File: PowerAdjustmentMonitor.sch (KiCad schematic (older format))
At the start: 18 parts, among them U3 LM317K, U4 7805, U5 7805, U6 LM317K, U7 LM324

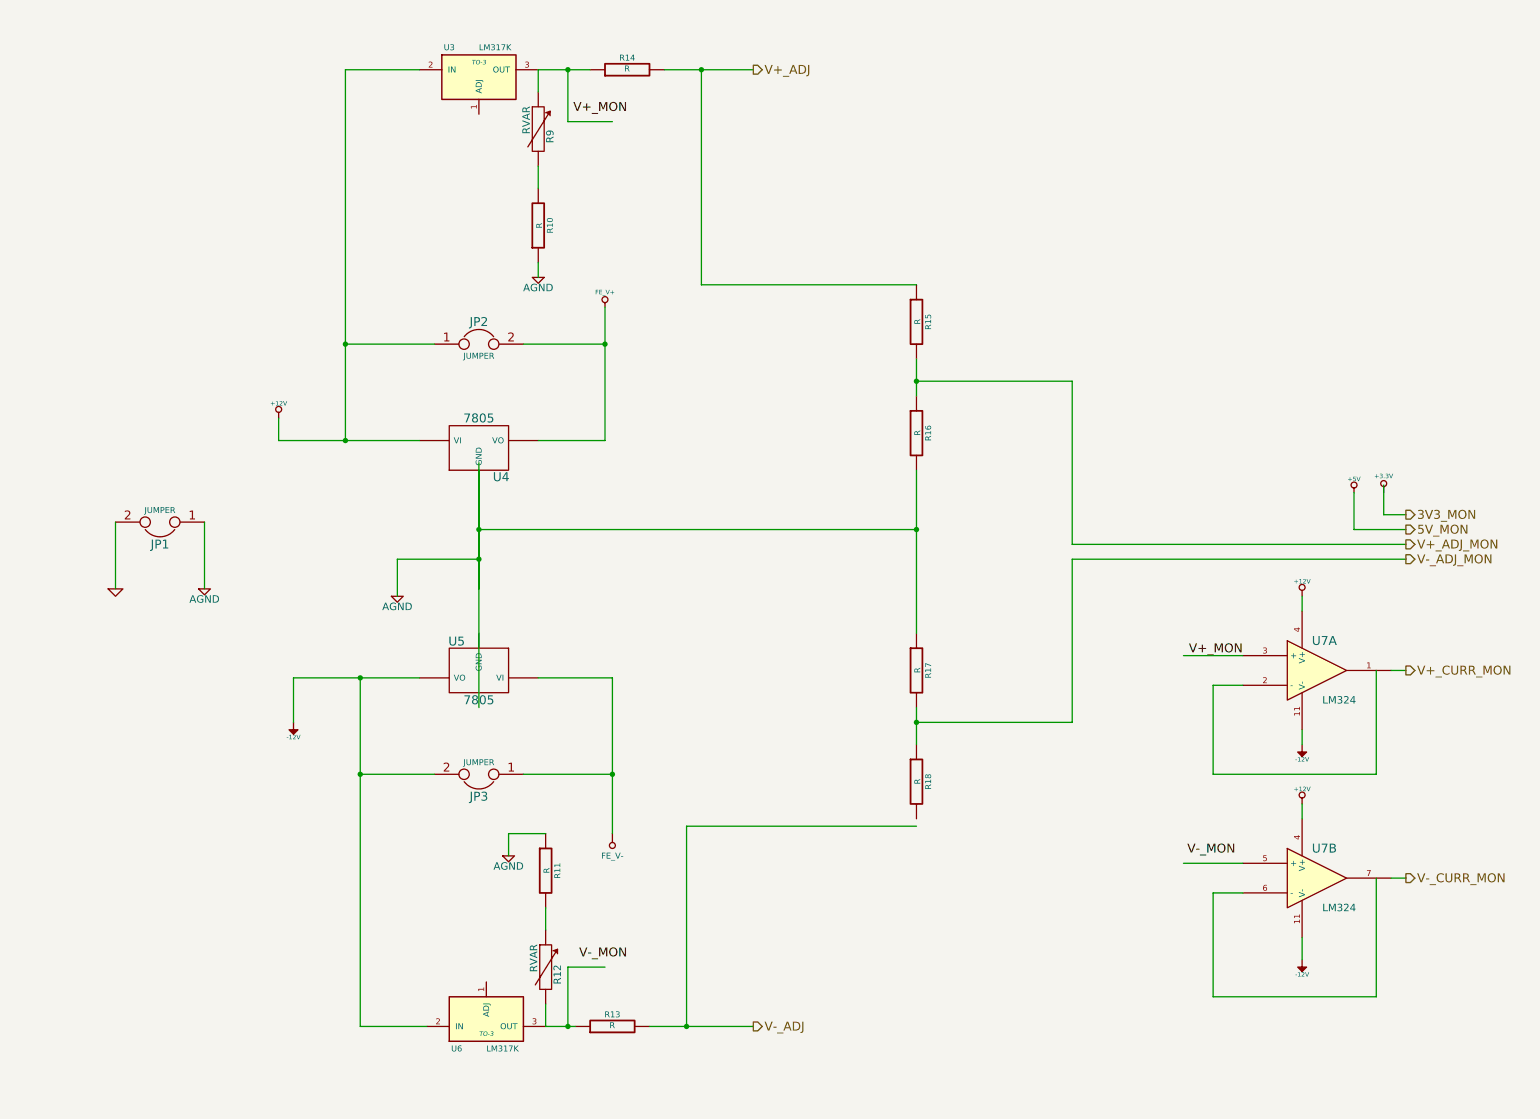
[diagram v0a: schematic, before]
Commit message: 5.4 Video 1/2 Associating and Placing the Thermocouple Module
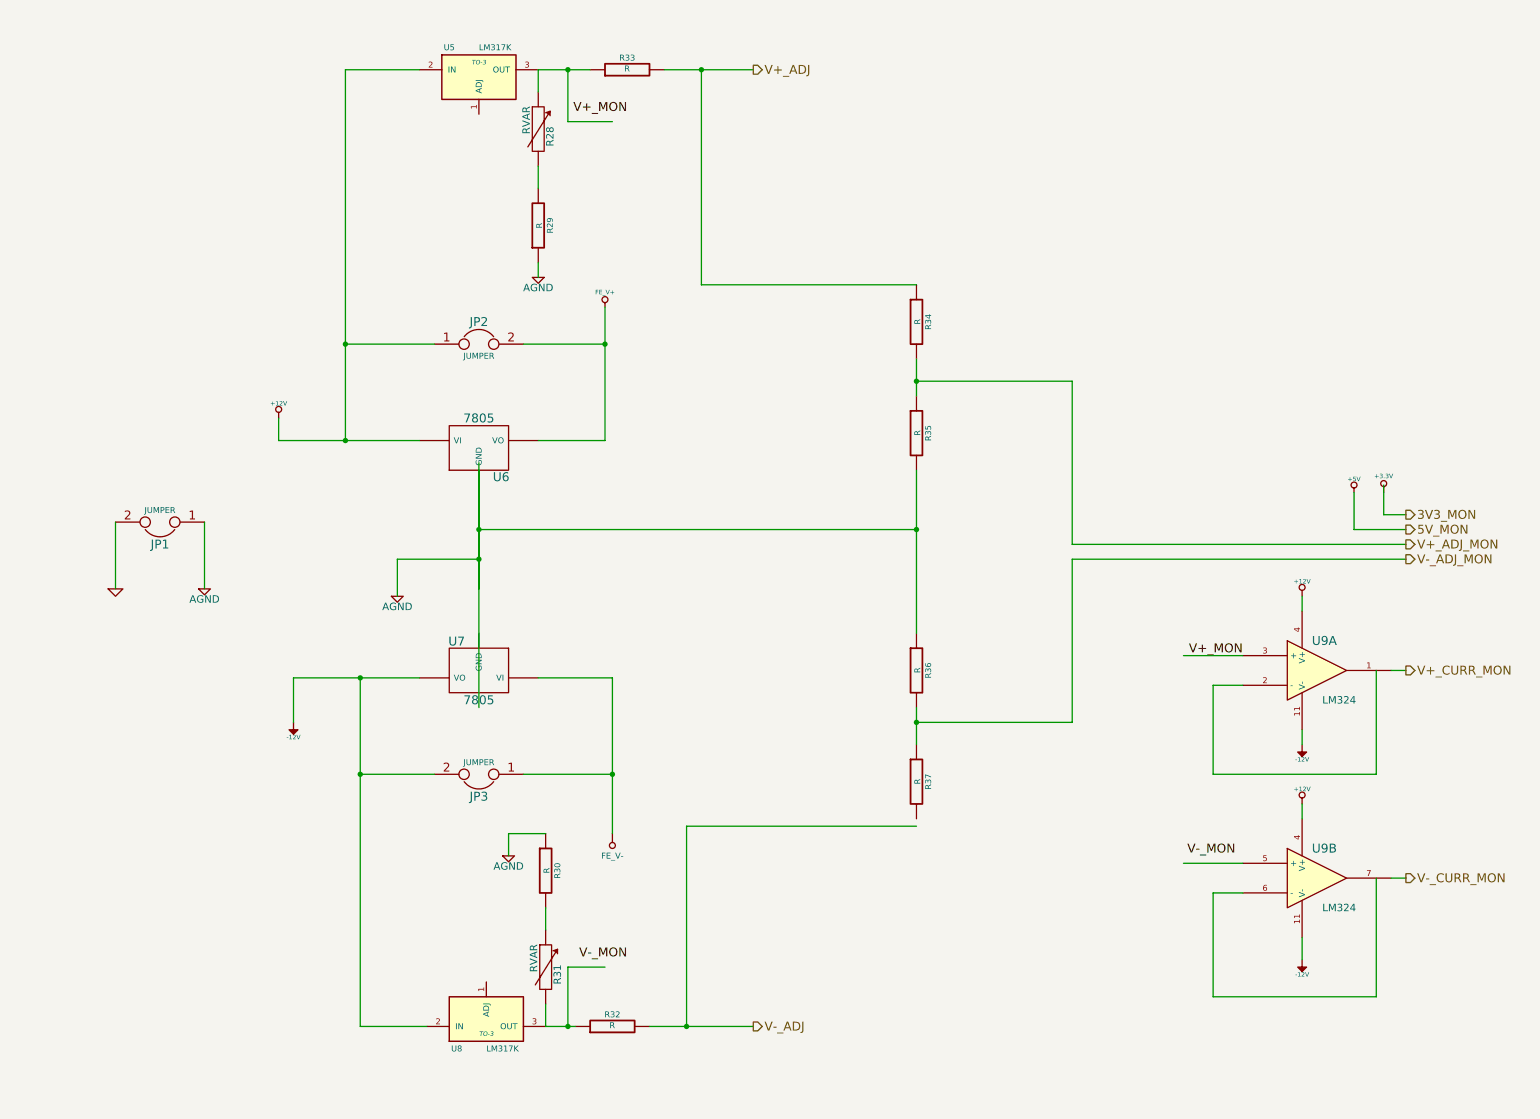
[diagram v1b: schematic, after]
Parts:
- renumbered R9 to R28, R10 to R29, R11 to R30, R12 to R31, R13 to R32, R14 to R33, R15 to R34, R16 to R35, R17 to R36, R18 to R37, U3 to U5, U4 to U6, U5 to U7, U6 to U8, U7 to U9
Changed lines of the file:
@@
 Sheet 9 9
 Title ""
-Date "19 feb 2014"
+Date "21 feb 2014"
 Rev ""
 Comp ""
@@
 $EndDescr
 $Comp
-L 7805 U4
+L 7805 U6
 U 1 1 52F50F52
 P 3850 3350
-F 0 "U4" H 4000 3154 60  0000 C CNN
+F 0 "U6" H 4000 3154 60  0000 C CNN
 F 1 "7805" H 3850 3550 60  0000 C CNN
 F 2 "" H 3850 3350 60  0000 C CNN
@@
 $EndComp
 $Comp
-L 7805 U5
+L 7805 U7
 U 1 1 52F50F5F
 P 3850 4850
-F 0 "U5" H 4000 4654 60  0000 C CNN
+F 0 "U7" H 4000 4654 60  0000 C CNN
 F 1 "7805" H 3850 5050 60  0000 C CNN
 F 2 "" H 3850 4850 60  0000 C CNN
@@
 $EndComp
 $Comp
-L R R11
+L R R30
 U 1 1 52F50F76
 P 4300 6200
-F 0 "R11" V 4380 6200 40  0000 C CNN
+F 0 "R30" V 4380 6200 40  0000 C CNN
 F 1 "R" V 4307 6201 40  0000 C CNN
 F 2 "" V 4230 6200 30  0000 C CNN
@@
 $EndComp
 $Comp
-L GND #PWR020
+L GND #PWR27
 U 1 1 52F50FA0
 P 1400 4300
-F 0 "#PWR020" H 1400 4300 30  0001 C CNN
+F 0 "#PWR27" H 1400 4300 30  0001 C CNN
 F 1 "GND" H 1400 4230 30  0001 C CNN
 F 2 "" H 1400 4300 60  0000 C CNN
@@
 $EndComp
 $Comp
-L AGND #PWR021
+L AGND #PWR28
 U 1 1 52F50FB9
 P 2000 4300
-F 0 "#PWR021" H 2000 4300 40  0001 C CNN
+F 0 "#PWR28" H 2000 4300 40  0001 C CNN
 F 1 "AGND" H 2000 4230 50  0000 C CNN
 F 2 "" H 2000 4300 60  0000 C CNN
@@
 $EndComp
 $Comp
-L AGND #PWR022
+L AGND #PWR31
 U 1 1 52F50FF4
 P 3300 4350
-F 0 "#PWR022" H 3300 4350 40  0001 C CNN
+F 0 "#PWR31" H 3300 4350 40  0001 C CNN
 F 1 "AGND" H 3300 4280 50  0000 C CNN
 F 2 "" H 3300 4350 60  0000 C CNN
@@
 $EndComp
 $Comp
-L +12V #PWR023
+L +12V #PWR29
 U 1 1 52F5102D
 P 2500 3150
-F 0 "#PWR023" H 2500 3100 20  0001 C CNN
+F 0 "#PWR29" H 2500 3100 20  0001 C CNN
 F 1 "+12V" H 2500 3250 30  0000 C CNN
 F 2 "" H 2500 3150 60  0000 C CNN
@@
 $EndComp
 $Comp
-L -12V #PWR024
+L -12V #PWR30
 U 1 1 52F5104F
 P 2600 5200
-F 0 "#PWR024" H 2600 5330 20  0001 C CNN
+F 0 "#PWR30" H 2600 5330 20  0001 C CNN
 F 1 "-12V" H 2600 5300 30  0000 C CNN
 F 2 "" H 2600 5200 60  0000 C CNN
@@
 $EndComp
 $Comp
-L FE_V+ #PWR025
+L FE_V+ #PWR34
 U 1 1 52F5159F
 P 4700 2400
-F 0 "#PWR025" H 4700 2500 30  0001 C CNN
+F 0 "#PWR34" H 4700 2500 30  0001 C CNN
 F 1 "FE_V+" H 4700 2500 30  0000 C CNN
 F 2 "" H 4700 2400 60  0000 C CNN
@@
 $EndComp
 $Comp
-L FE_V- #PWR28
+L FE_V- #PWR35
 U 1 1 52F515C8
 P 4750 5950
-F 0 "#PWR28" H 4750 6150 40  0001 C CNN
+F 0 "#PWR35" H 4750 6150 40  0001 C CNN
 F 1 "FE_V-" H 4750 6100 40  0000 C CNN
 F 2 "" H 4750 5950 60  0000 C CNN
@@
 $EndComp
 $Comp
-L LM317K U6
+L LM317K U8
 U 1 1 52F51657
 P 3900 7200
-F 0 "U6" H 3700 7400 40  0000 C CNN
+F 0 "U8" H 3700 7400 40  0000 C CNN
 F 1 "LM317K" H 3900 7400 40  0000 L CNN
 F 2 "TO-3" H 3900 7300 30  0000 C CIN
@@
 $EndComp
 $Comp
-L AGND #PWR026
+L AGND #PWR32
 U 1 1 52F516D6
 P 4050 6100
-F 0 "#PWR026" H 4050 6100 40  0001 C CNN
+F 0 "#PWR32" H 4050 6100 40  0001 C CNN
 F 1 "AGND" H 4050 6030 50  0000 C CNN
 F 2 "" H 4050 6100 60  0000 C CNN
@@
 $EndComp
 $Comp
-L R R10
+L R R29
 U 1 1 52F51728
 P 4250 1850
-F 0 "R10" V 4330 1850 40  0000 C CNN
+F 0 "R29" V 4330 1850 40  0000 C CNN
 F 1 "R" V 4257 1851 40  0000 C CNN
 F 2 "" V 4180 1850 30  0000 C CNN
@@
 $EndComp
 $Comp
-L LM317K U3
+L LM317K U5
 U 1 1 52F5172F
 P 3850 850
-F 0 "U3" H 3650 1050 40  0000 C CNN
+F 0 "U5" H 3650 1050 40  0000 C CNN
 F 1 "LM317K" H 3850 1050 40  0000 L CNN
 F 2 "TO-3" H 3850 950 30  0000 C CIN
@@
 $EndComp
 $Comp
-L AGND #PWR027
+L AGND #PWR33
 U 1 1 52F51738
 P 4250 2200
-F 0 "#PWR027" H 4250 2200 40  0001 C CNN
+F 0 "#PWR33" H 4250 2200 40  0001 C CNN
 F 1 "AGND" H 4250 2130 50  0000 C CNN
 F 2 "" H 4250 2200 60  0000 C CNN
@@
 V-_ADJ
 $Comp
-L +3.3V #PWR028
+L +3.3V #PWR41
 U 1 1 52F517F0
 P 9950 3650
-F 0 "#PWR028" H 9950 3610 30  0001 C CNN
+F 0 "#PWR41" H 9950 3610 30  0001 C CNN
 F 1 "+3.3V" H 9950 3760 30  0000 C CNN
 F 2 "" H 9950 3650 60  0000 C CNN
@@
 V-_ADJ_MON
 $Comp
-L +5V #PWR029
+L +5V #PWR40
 U 1 1 52F51806
 P 9750 3650
-F 0 "#PWR029" H 9750 3740 20  0001 C CNN
+F 0 "#PWR40" H 9750 3740 20  0001 C CNN
 F 1 "+5V" H 9750 3740 30  0000 C CNN
 F 2 "" H 9750 3650 60  0000 C CNN
@@
 V-_CURR_MON
 $Comp
-L R R15
+L R R34
 U 1 1 52F5181A
 P 6800 2500
-F 0 "R15" V 6880 2500 40  0000 C CNN
+F 0 "R34" V 6880 2500 40  0000 C CNN
 F 1 "R" V 6807 2501 40  0000 C CNN
 F 2 "" V 6730 2500 30  0000 C CNN
@@
 $EndComp
 $Comp
-L R R16
+L R R35
 U 1 1 52F5182D
 P 6800 3250
-F 0 "R16" V 6880 3250 40  0000 C CNN
+F 0 "R35" V 6880 3250 40  0000 C CNN
 F 1 "R" V 6807 3251 40  0000 C CNN
 F 2 "" V 6730 3250 30  0000 C CNN
@@
 	6800 2750 6800 3000
 $Comp
-L R R17
+L R R36
 U 1 1 52F51905
 P 6800 4850
-F 0 "R17" V 6880 4850 40  0000 C CNN
+F 0 "R36" V 6880 4850 40  0000 C CNN
 F 1 "R" V 6807 4851 40  0000 C CNN
 F 2 "" V 6730 4850 30  0000 C CNN
@@
 $EndComp
 $Comp
-L R R18
+L R R37
 U 1 1 52F5190B
 P 6800 5600
-F 0 "R18" V 6880 5600 40  0000 C CNN
+F 0 "R37" V 6880 5600 40  0000 C CNN
 F 1 "R" V 6807 5601 40  0000 C CNN
 F 2 "" V 6730 5600 30  0000 C CNN
@@
 	9750 3900 10100 3900
 $Comp
-L R R13
+L R R32
 U 1 1 52F51ABE
 P 4750 7250
-F 0 "R13" V 4830 7250 40  0000 C CNN
+F 0 "R32" V 4830 7250 40  0000 C CNN
 F 1 "R" V 4757 7251 40  0000 C CNN
 F 2 "" V 4680 7250 30  0000 C CNN
@@
 	4300 7250 4500 7250
 $Comp
-L R R14
+L R R33
 U 1 1 52F51B5C
 P 4850 800
-F 0 "R14" V 4930 800 40  0000 C CNN
+F 0 "R33" V 4930 800 40  0000 C CNN
 F 1 "R" V 4857 801 40  0000 C CNN
 F 2 "" V 4780 800 30  0000 C CNN
@@
 V+_MON
 $Comp
-L LM324 U7
+L LM324 U9
 U 1 1 52F51E74
 P 9500 4850
-F 0 "U7" H 9550 5050 60  0000 C CNN
+F 0 "U9" H 9550 5050 60  0000 C CNN
 F 1 "LM324" H 9650 4650 50  0000 C CNN
 F 2 "" H 9500 4850 60  0000 C CNN
@@
 $EndComp
 $Comp
-L LM324 U7
+L LM324 U9
 U 2 1 52F51E7A
 P 9500 6250
-F 0 "U7" H 9550 6450 60  0000 C CNN
+F 0 "U9" H 9550 6450 60  0000 C CNN
 F 1 "LM324" H 9650 6050 50  0000 C CNN
 F 2 "" H 9500 6250 60  0000 C CNN
@@
 	10000 6250 10100 6250
 $Comp
-L +12V #PWR030
+L +12V #PWR36
 U 1 1 52F51F5F
 P 9400 4350
-F 0 "#PWR030" H 9400 4300 20  0001 C CNN
+F 0 "#PWR36" H 9400 4300 20  0001 C CNN
 F 1 "+12V" H 9400 4450 30  0000 C CNN
 F 2 "" H 9400 4350 60  0000 C CNN
@@
 	9400 4350 9400 4450
 $Comp
-L +12V #PWR031
+L +12V #PWR38
 U 1 1 52F51FC1
 P 9400 5750
-F 0 "#PWR031" H 9400 5700 20  0001 C CNN
+F 0 "#PWR38" H 9400 5700 20  0001 C CNN
 F 1 "+12V" H 9400 5850 30  0000 C CNN
 F 2 "" H 9400 5750 60  0000 C CNN
@@
 	9400 5750 9400 5850
 $Comp
-L -12V #PWR032
+L -12V #PWR37
 U 1 1 52F5201F
 P 9400 5350
-F 0 "#PWR032" H 9400 5480 20  0001 C CNN
+F 0 "#PWR37" H 9400 5480 20  0001 C CNN
 F 1 "-12V" H 9400 5450 30  0000 C CNN
 F 2 "" H 9400 5350 60  0000 C CNN
@@
 	9400 5250 9400 5350
 $Comp
-L -12V #PWR033
+L -12V #PWR39
 U 1 1 52F5207B
 P 9400 6800
-F 0 "#PWR033" H 9400 6930 20  0001 C CNN
+F 0 "#PWR39" H 9400 6930 20  0001 C CNN
 F 1 "-12V" H 9400 6900 30  0000 C CNN
 F 2 "" H 9400 6800 60  0000 C CNN
@@
 V-_MON
 $Comp
-L RVAR R12
+L RVAR R31
 U 1 1 52F526E6
 P 4300 6850
-F 0 "R12" V 4380 6800 50  0000 C CNN
+F 0 "R31" V 4380 6800 50  0000 C CNN
 F 1 "RVAR" V 4220 6910 50  0000 C CNN
 F 2 "" H 4300 6850 60  0000 C CNN
@@
 $EndComp
 $Comp
-L RVAR R9
+L RVAR R28
 U 1 1 52F526F3
 P 4250 1200
-F 0 "R9" V 4330 1150 50  0000 C CNN
+F 0 "R28" V 4330 1150 50  0000 C CNN
 F 1 "RVAR" V 4170 1260 50  0000 C CNN
 F 2 "" H 4250 1200 60  0000 C CNN

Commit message: 5.10 Video 1/2 Associating and Placing the Power Modification Module
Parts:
- removed JP2, JP3: JUMPER, symbol JUMPER
- removed U6, U7: 7805, symbol 7805
- removed U8: LM317K, TO-3, symbol LM317K
- removed U9: LM324, symbol LM324
- added C14, C15, C16, C17, C18, C19, C20, C21, C22, C23, C24, C25: C, ~, symbol C
- added D10, D5, D6, D7, D8, D9: DIODE, ~, symbol DIODE
- added R54, R55: R, ~, symbol R
- added U6, U7: LM337T, TO-220, symbol LM337T
- added U8: LM317, ~, symbol LM317
- R30, R32, R33: footprint (none) -> ~
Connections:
- net labels removed: V+_CURR_MON, V-_CURR_MON, V-_MON
- wire segments 71 -> 93
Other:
- note added: "- 1.5 to 10V Output"
- note added: "-10V Output"
- note added: "1.5 to 10 V Output"
- note added: "10V Output"
- moved on the sheet: JP1, R28, R29

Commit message: 5.10 Video 2/2 Associating and Placing the Power Modification Module
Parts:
- added D11, D12: MMBD914-7-F, ~, symbol DIODE
- D10, D5, D6, D7, D8, D9: value DIODE -> MMBD914-7-F
- R28: value RVAR -> 5K
- R29, R30: value R -> 715
- R31: value RVAR -> 5k
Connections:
- wire segments 93 -> 101
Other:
- moved on the sheet: D7
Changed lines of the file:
@@
 Sheet 8 9
 Title ""
-Date "23 feb 2014"
+Date "24 feb 2014"
 Rev ""
 Comp ""
@@
 $EndComp
 $Comp
-L GND #PWR39
+L GND #PWR038
 U 1 1 52F50FA0
 P 800 3900
-F 0 "#PWR39" H 800 3900 30  0001 C CNN
+F 0 "#PWR038" H 800 3900 30  0001 C CNN
 F 1 "GND" H 800 3830 30  0001 C CNN
 F 2 "" H 800 3900 60  0000 C CNN
@@
 $EndComp
 $Comp
-L AGND #PWR40
+L AGND #PWR039
 U 1 1 52F50FB9
 P 1400 3900
-F 0 "#PWR40" H 1400 3900 40  0001 C CNN
+F 0 "#PWR039" H 1400 3900 40  0001 C CNN
 F 1 "AGND" H 1400 3830 50  0000 C CNN
 F 2 "" H 1400 3900 60  0000 C CNN
@@
 $EndComp
 $Comp
-L AGND #PWR42
+L AGND #PWR040
 U 1 1 52F50FF4
 P 2300 4150
-F 0 "#PWR42" H 2300 4150 40  0001 C CNN
+F 0 "#PWR040" H 2300 4150 40  0001 C CNN
 F 1 "AGND" H 2300 4080 50  0000 C CNN
 F 2 "" H 2300 4150 60  0000 C CNN
@@
 $EndComp
 $Comp
-L +12V #PWR41
+L +12V #PWR041
 U 1 1 52F5102D
 P 2300 650
-F 0 "#PWR41" H 2300 600 20  0001 C CNN
+F 0 "#PWR041" H 2300 600 20  0001 C CNN
 F 1 "+12V" H 2300 750 30  0000 C CNN
 F 2 "" H 2300 650 60  0000 C CNN
@@
 $EndComp
 $Comp
-L -12V #PWR43
+L -12V #PWR042
 U 1 1 52F5104F
 P 2300 5350
-F 0 "#PWR43" H 2300 5480 20  0001 C CNN
+F 0 "#PWR042" H 2300 5480 20  0001 C CNN
 F 1 "-12V" H 2300 5450 30  0000 C CNN
 F 2 "" H 2300 5350 60  0000 C CNN
@@
 P 4300 1200
 F 0 "R29" V 4380 1200 40  0000 C CNN
-F 1 "R" V 4307 1201 40  0000 C CNN
+F 1 "715" V 4307 1201 40  0000 C CNN
 F 2 "" V 4230 1200 30  0000 C CNN
 F 3 "" H 4300 1200 30  0000 C CNN
@@
 $EndComp
 $Comp
-L AGND #PWR46
+L AGND #PWR043
 U 1 1 52F51738
 P 4300 2200
-F 0 "#PWR46" H 4300 2200 40  0001 C CNN
+F 0 "#PWR043" H 4300 2200 40  0001 C CNN
 F 1 "AGND" H 4300 2130 50  0000 C CNN
 F 2 "" H 4300 2200 60  0000 C CNN
@@
 V-_ADJ
 $Comp
-L +3.3V #PWR50
+L +3.3V #PWR044
 U 1 1 52F517F0
 P 9950 3650
-F 0 "#PWR50" H 9950 3610 30  0001 C CNN
+F 0 "#PWR044" H 9950 3610 30  0001 C CNN
 F 1 "+3.3V" H 9950 3760 30  0000 C CNN
 F 2 "" H 9950 3650 60  0000 C CNN
@@
 V-_ADJ_MON
 $Comp
-L +5V #PWR49
+L +5V #PWR045
 U 1 1 52F51806
 P 9750 3650
-F 0 "#PWR49" H 9750 3740 20  0001 C CNN
+F 0 "#PWR045" H 9750 3740 20  0001 C CNN
 F 1 "+5V" H 9750 3740 30  0000 C CNN
 F 2 "" H 9750 3650 60  0000 C CNN
@@
 P 4300 1850
 F 0 "R28" V 4380 1800 50  0000 C CNN
-F 1 "RVAR" V 4220 1910 50  0000 C CNN
+F 1 "5K" V 4220 1910 50  0000 C CNN
 F 2 "" H 4300 1850 60  0000 C CNN
 F 3 "" H 4300 1850 60  0000 C CNN
@@
 $EndComp
 $Comp
-L FE_V+ #PWR47
+L FE_V+ #PWR046
 U 1 1 530A7BE6
 P 5150 2550
-F 0 "#PWR47" H 5150 2650 30  0001 C CNN
+F 0 "#PWR046" H 5150 2650 30  0001 C CNN
 F 1 "FE_V+" H 5150 2650 30  0000 C CNN
 F 2 "~" H 5150 2550 60  0000 C CNN
@@
 Text Notes 4250 600  0    60   ~ 0
 1.5 to 10 V Output
-Text Notes 5050 2800 0    60   ~ 0
+Text Notes 5250 2550 0    60   ~ 0
 10V Output
 $Comp
@@
 P 3950 7150
 F 0 "R30" V 4030 7150 40  0000 C CNN
-F 1 "R" V 3957 7151 40  0000 C CNN
+F 1 "715" V 3957 7151 40  0000 C CNN
 F 2 "~" V 3880 7150 30  0000 C CNN
 F 3 "~" H 3950 7150 30  0000 C CNN
@@
 $EndComp
 $Comp
-L AGND #PWR45
+L AGND #PWR047
 U 1 1 530A7F80
 P 3400 6250
-F 0 "#PWR45" H 3400 6250 40  0001 C CNN
+F 0 "#PWR047" H 3400 6250 40  0001 C CNN
 F 1 "AGND" H 3400 6180 50  0000 C CNN
 F 2 "" H 3400 6250 60  0000 C CNN
@@
 P 3950 6400
 F 0 "R31" V 4030 6350 50  0000 C CNN
-F 1 "RVAR" V 3870 6460 50  0000 C CNN
+F 1 "5k" V 3870 6460 50  0000 C CNN
 F 2 "" H 3950 6400 60  0000 C CNN
 F 3 "" H 3950 6400 60  0000 C CNN
@@
 $EndComp
 $Comp
-L AGND #PWR44
+L AGND #PWR048
 U 1 1 530A8E3E
 P 3000 1600
-F 0 "#PWR44" H 3000 1600 40  0001 C CNN
+F 0 "#PWR048" H 3000 1600 40  0001 C CNN
 F 1 "AGND" H 3000 1530 50  0000 C CNN
 F 2 "" H 3000 1600 60  0000 C CNN
@@
 P 4650 1150
 F 0 "D9" H 4650 1250 40  0000 C CNN
-F 1 "DIODE" H 4650 1050 40  0000 C CNN
+F 1 "MMBD914-7-F" H 4650 1050 40  0000 C CNN
 F 2 "~" H 4650 1150 60  0000 C CNN
 F 3 "~" H 4650 1150 60  0000 C CNN
@@
 P 3850 550
 F 0 "D5" H 3850 650 40  0000 C CNN
-F 1 "DIODE" H 3850 450 40  0000 C CNN
+F 1 "MMBD914-7-F" H 3850 450 40  0000 C CNN
 F 2 "~" H 3850 550 60  0000 C CNN
 F 3 "~" H 3850 550 60  0000 C CNN
@@
 P 4050 2400
 F 0 "D6" H 4050 2500 40  0000 C CNN
-F 1 "DIODE" H 4050 2300 40  0000 C CNN
+F 1 "MMBD914-7-F" H 4050 2300 40  0000 C CNN
 F 2 "~" H 4050 2400 60  0000 C CNN
 F 3 "~" H 4050 2400 60  0000 C CNN
@@
 P 4950 2900
 F 0 "D10" H 4950 3000 40  0000 C CNN
-F 1 "DIODE" H 4950 2800 40  0000 C CNN
+F 1 "MMBD914-7-F" H 4950 2800 40  0000 C CNN
 F 2 "~" H 4950 2900 60  0000 C CNN
 F 3 "~" H 4950 2900 60  0000 C CNN
@@
 	0    -1   -1   0
 $EndComp
+$Comp
+L DIODE D7
+U 1 1 530A9FC3
+P 4600 4450
+F 0 "D7" H 4600 4550 40  0000 C CNN
+F 1 "MMBD914-7-F" H 4600 4350 40  0000 C CNN
+F 2 "~" H 4600 4450 60  0000 C CNN
+F 3 "~" H 4600 4450 60  0000 C CNN
+	1    4600 4450
+	0    -1   -1   0
+$EndComp
+$Comp
+L DIODE D8
+U 1 1 530AA2B6
+P 4600 7100
+F 0 "D8" H 4600 7200 40  0000 C CNN
+F 1 "MMBD914-7-F" H 4600 7000 40  0000 C CNN
+F 2 "~" H 4600 7100 60  0000 C CNN
+F 3 "~" H 4600 7100 60  0000 C CNN
+	1    4600 7100
+	0    -1   -1   0
+$EndComp
 Wire Wire Line
 	1400 3600 1400 3900
@@
 	9750 3900 10100 3900
 Wire Wire Line
-	4250 800  5150 800
-Wire Wire Line
-	5350 800  5700 800
+	4250 800  5700 800
 Wire Wire Line
 	4450 800  4450 700
@@
 Wire Wire Line
 	5150 5350 5150 6450
-Connection ~ 4600 5600
 Wire Wire Line
 	5150 6850 5150 7550
@@
 Wire Wire Line
 	4950 3200 4950 3100
-$Comp
-L DIODE D7
-U 1 1 530A9FC3
-P 4600 5150
-F 0 "D7" H 4600 5250 40  0000 C CNN
-F 1 "DIODE" H 4600 5050 40  0000 C CNN
-F 2 "~" H 4600 5150 60  0000 C CNN
-F 3 "~" H 4600 5150 60  0000 C CNN
-	1    4600 5150
-	0    1    1    0
-$EndComp
-Wire Wire Line
-	4600 4800 4600 4950
-Wire Wire Line
-	4600 5350 4600 5600
-$Comp
-L DIODE D8
-U 1 1 530AA2B6
-P 4600 7100
-F 0 "D8" H 4600 7200 40  0000 C CNN
-F 1 "DIODE" H 4600 7000 40  0000 C CNN
-F 2 "~" H 4600 7100 60  0000 C CNN
-F 3 "~" H 4600 7100 60  0000 C CNN
-	1    4600 7100
-	0    1    1    0
-$EndComp
 Wire Wire Line
 	4600 6750 4600 6900
 Wire Wire Line
 	4600 7300 4600 7550
+Connection ~ 5150 800
+Wire Wire Line
+	4600 4800 4600 4650
+Wire Wire Line
+	4600 4250 4600 3900
+Connection ~ 4600 3900
+$Comp
+L DIODE D12
+U 1 1 530AB60E
+P 3450 5900
+F 0 "D12" H 3450 6000 40  0000 C CNN
+F 1 "MMBD914-7-F" H 3450 5800 40  0000 C CNN
+F 2 "~" H 3450 5900 60  0000 C CNN
+F 3 "~" H 3450 5900 60  0000 C CNN
+	1    3450 5900
+	-1   0    0    1
+$EndComp
+Wire Wire Line
+	3250 5900 2900 5900
+Wire Wire Line
+	2900 5900 2900 5600
+Connection ~ 2900 5600
+Wire Wire Line
+	3650 5900 4050 5900
+Wire Wire Line
+	4050 5900 4050 5600
+Connection ~ 4050 5600
+$Comp
+L DIODE D11
+U 1 1 530AB71B
+P 2200 7650
+F 0 "D11" H 2200 7750 40  0000 C CNN
+F 1 "MMBD914-7-F" H 2200 7550 40  0000 C CNN
+F 2 "~" H 2200 7650 60  0000 C CNN
+F 3 "~" H 2200 7650 60  0000 C CNN
+	1    2200 7650
+	-1   0    0    1
+$EndComp
+Connection ~ 3700 7550
+Wire Wire Line
+	3700 7550 3700 7750
+Wire Wire Line
+	3700 7750 2400 7750
+Wire Wire Line
+	2400 7750 2400 7650
+Wire Wire Line
+	2000 7650 2000 7250
+Wire Wire Line
+	2000 7250 2500 7250
+Connection ~ 2500 7250
 $EndSCHEMATC
